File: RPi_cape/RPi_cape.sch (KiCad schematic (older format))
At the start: 110 parts, among them J1 Conn_01x04, J10 Conn_01x02, J11 Conn_01x02, J12 Conn_01x02, J15 Conn_01x06, J16 Conn_01x06, J2 Conn_01x02, J21 Conn_01x06, J3 Conn_01x02, J4 Conn_01x02, J5 Conn_01x03, J6 Conn_01x03, J7 Conn_01x02, J8 Conn_02x20_Odd_Even, J9 Conn_01x02, U1 TL431A, U2 ADC128D818, U3 ADC128D818

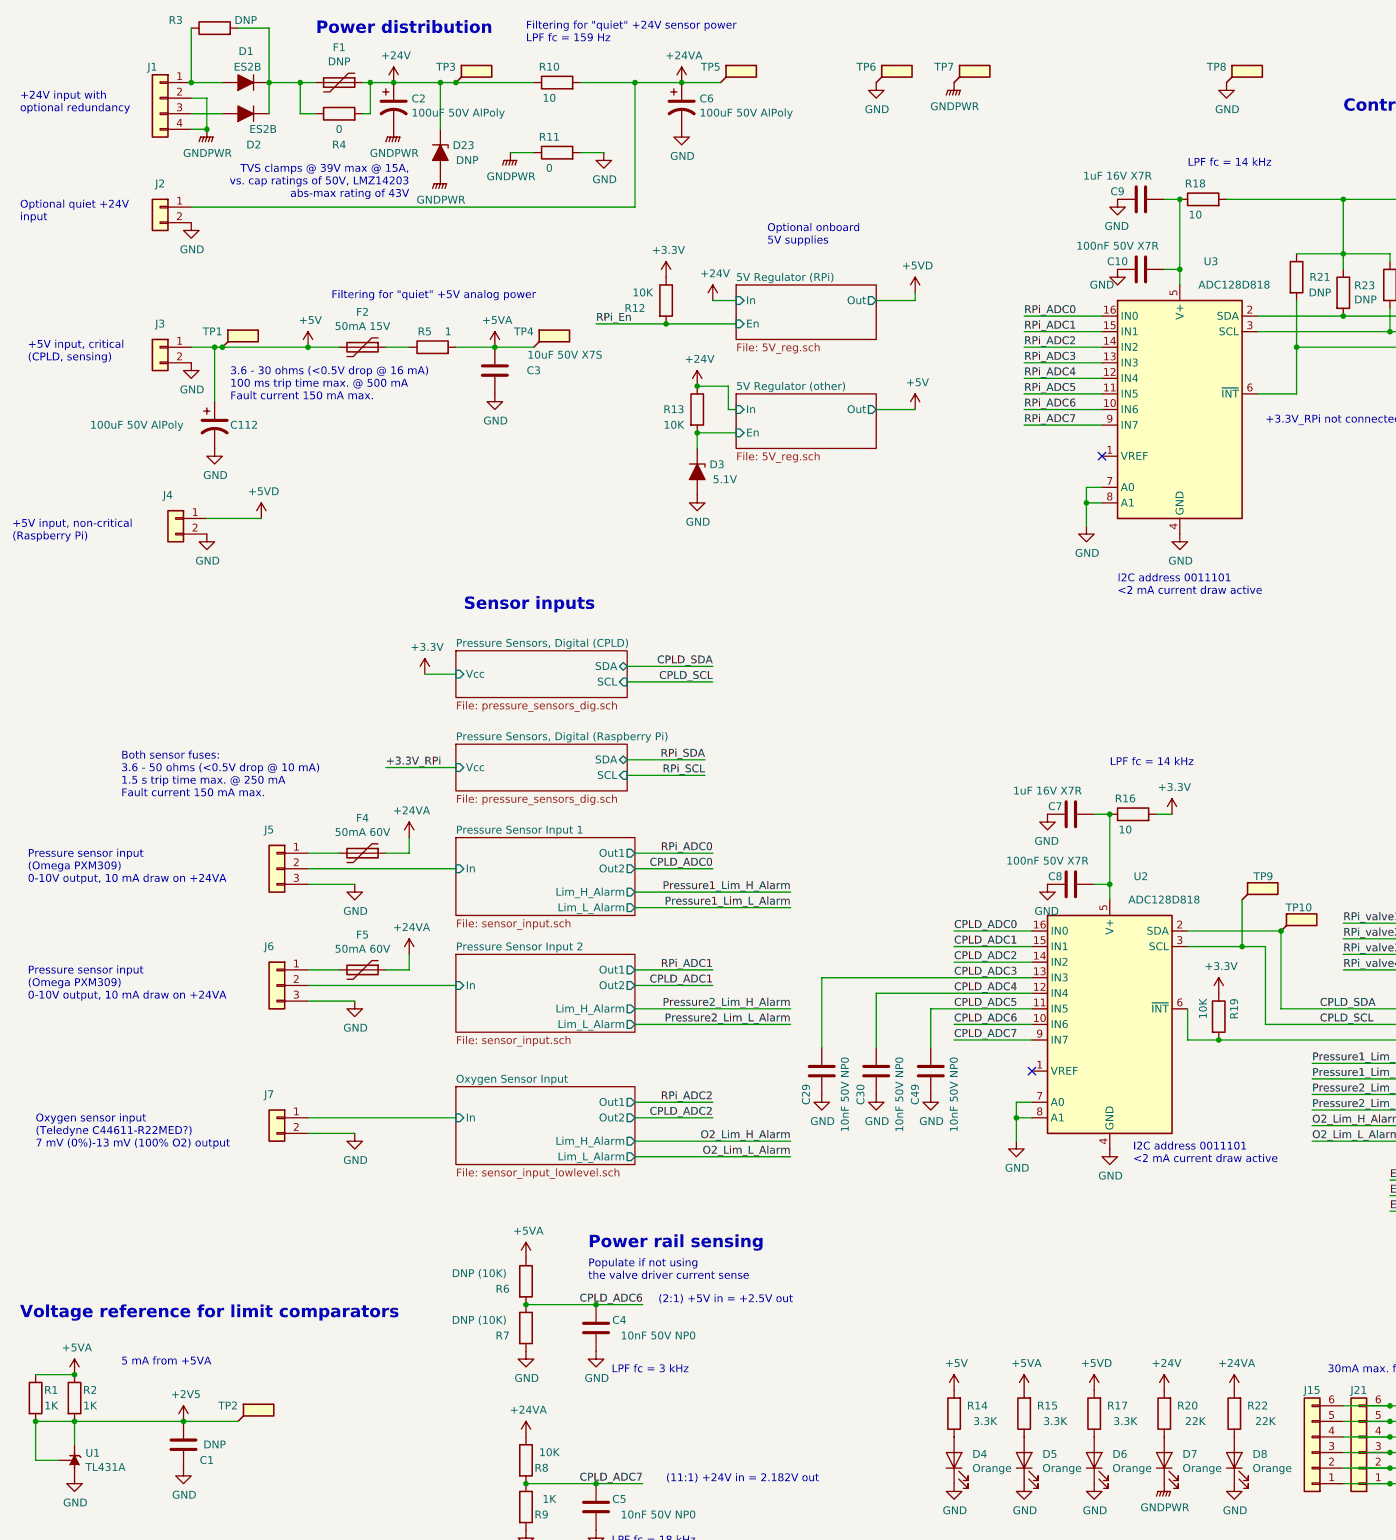
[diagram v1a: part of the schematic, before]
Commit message: Updates based on testing, extra documentation
Added thermal calculations, possible thermal-induced problems to fault-condition list
Renamed error calculations file
Added some bringup tests
Changed 24V LED resistors (R20, R22) to 24.9K to consolidate BOM
Adjusted audio amp volume and filtering according to breadboard experiments
Moved bottom-end mounting holes and encoder connectors to avoid interfering mechanically with Raspberry Pi
Replaced under-sized power-ORing diodes with better Schottky option, added heatsinking with copper planes
Improved LMZ14203 heatsinking by removing thermal reliefs, re-arranging input-current-measurement testpoints to increase top-layer copper area
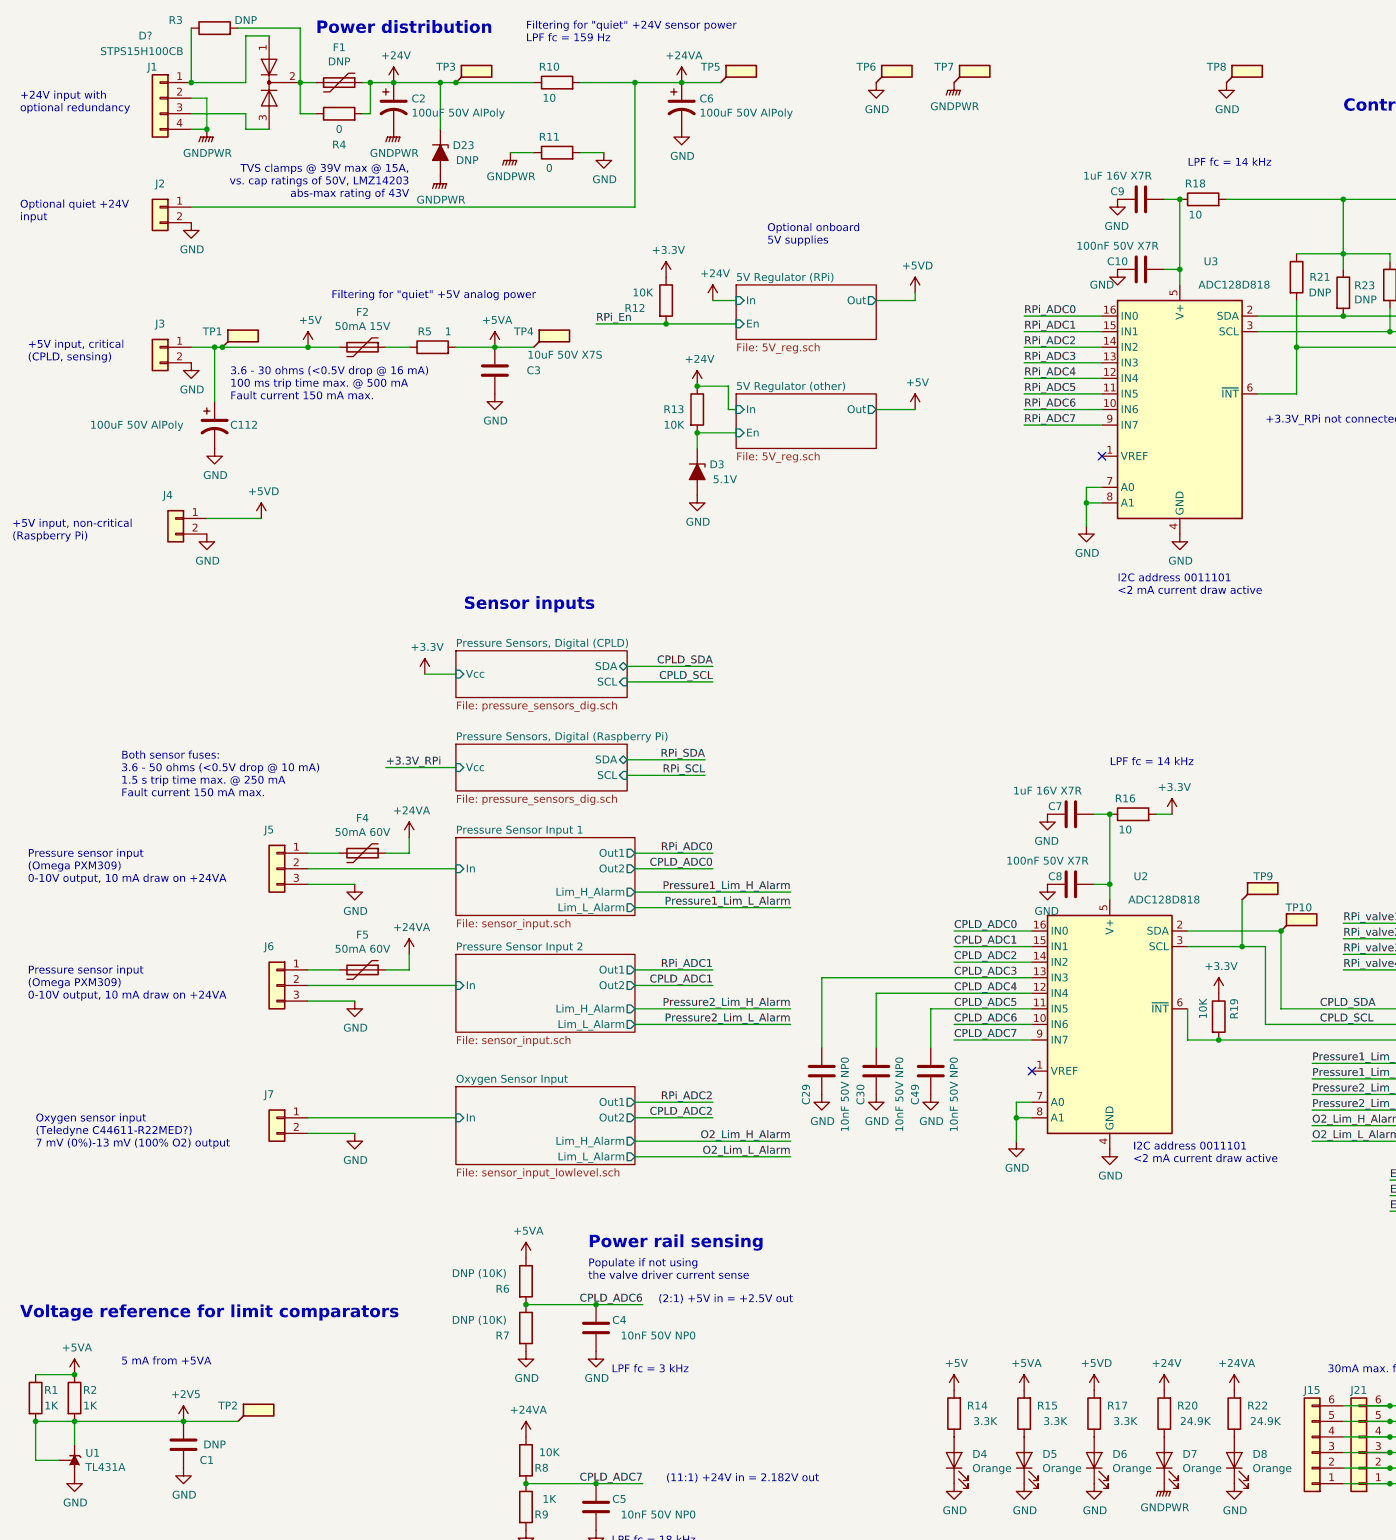
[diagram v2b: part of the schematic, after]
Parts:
- removed D1, D2: ES2B, Ventilator:D_SMA, symbol Device:D_ALT
- added D?: STPS15H100CB, Package_TO_SOT_SMD:TO-252-2, symbol Device:D_x2_KCom_AKA
- R20, R22: value 22K -> 24.9K; Part Number RK73H2BTTD2202F -> RK73H2BTTD2492F
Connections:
- net at J1.1 (Pin_1), R3.1: now also D?.1 (A)
- net at J1.3 (Pin_3): now also D?.3 (A)
- net at F1.2, R3.2, R4.1: now also D?.2 (K)
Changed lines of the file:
@@
 Title "Raspberry Pi Hat for JamVent Adaptation"
 Date ""
-Rev "1.8"
+Rev "1.9"
 Comp "US JamVent Team"
 Comment1 "Don Straney"
@@
 Connection ~ 1750 1250
 $Comp
-L Device:D_ALT D?
-U 1 1 5E93929F
-P 2000 950
-AR Path="/5E8FBD97/5E93929F" Ref="D?"  Part="1"
-AR Path="/5E8DEDC0/5E93929F" Ref="D?"  Part="1"
-AR Path="/5E8DFCAD/5E93929F" Ref="D?"  Part="1"
-AR Path="/5E8E0754/5E93929F" Ref="D?"  Part="1"
-AR Path="/5E93929F" Ref="D1"  Part="1"
-F 0 "D1" H 1950 750 50  0000 L CNN
-F 1 "ES2B" H 1900 850 50  0000 L CNN
-F 2 "Ventilator:D_SMA" H 2000 950 50  0001 C CNN
-F 3 "~" H 2000 950 50  0001 C CNN
-F 4 "Vishay" H 2000 950 50  0001 C CNN "Manufacturer"
-F 5 "ES2G-E3/52T" H 2000 950 50  0001 C CNN "Part Number"
-	1    2000 950
-	-1   0    0    1
-$EndComp
-Wire Wire Line
-	1850 950  1650 950
-$Comp
-L Device:D_ALT D?
-U 1 1 5E93B9F0
-P 2000 1150
-AR Path="/5E8FBD97/5E93B9F0" Ref="D?"  Part="1"
-AR Path="/5E8DEDC0/5E93B9F0" Ref="D?"  Part="1"
-AR Path="/5E8DFCAD/5E93B9F0" Ref="D?"  Part="1"
-AR Path="/5E8E0754/5E93B9F0" Ref="D?"  Part="1"
-AR Path="/5E93B9F0" Ref="D2"  Part="1"
-F 0 "D2" H 1900 1350 50  0000 L CNN
-F 1 "ES2B" H 1800 1250 50  0000 L CNN
-F 2 "Ventilator:D_SMA" H 2000 1150 50  0001 C CNN
-F 3 "~" H 2000 1150 50  0001 C CNN
-F 4 "Vishay" H 2000 1150 50  0001 C CNN "Manufacturer"
-F 5 "ES2G-E3/52T" H 2000 1150 50  0001 C CNN "Part Number"
-	1    2000 1150
-	-1   0    0    1
-$EndComp
-Wire Wire Line
-	1650 1150 1850 1150
-Wire Wire Line
-	2150 1150 2150 950
-Wire Wire Line
-	2150 950  2350 950
-Connection ~ 2150 950
-$Comp
 L Device:R R10
 U 1 1 5E9432CB
@@
 $EndComp
 Wire Wire Line
-	1950 600  2150 600
-Wire Wire Line
-	2150 600  2150 950
-Wire Wire Line
 	1650 600  1650 950
 Connection ~ 1650 950
@@
 AR Path="/5E8C8865/5F731777" Ref="R?"  Part="1"
 F 0 "R20" H 7750 9450 50  0000 C CNN
-F 1 "22K" H 7700 9550 50  0000 C CNN
+F 1 "24.9K" H 7700 9550 50  0000 C CNN
 F 2 "Resistor_SMD:R_1206_3216Metric" V 7830 9500 50  0001 C CNN
 F 3 "~" H 7900 9500 50  0001 C CNN
 F 4 "KOA Speer" H 7900 9500 50  0001 C CNN "Manufacturer"
-F 5 "RK73H2BTTD2202F" H 7900 9500 50  0001 C CNN "Part Number"
+F 5 "RK73H2BTTD2492F" H 7900 9500 50  0001 C CNN "Part Number"
 	1    7900 9500
 	-1   0    0    1
@@
 AR Path="/5E8C8865/5F747055" Ref="R?"  Part="1"
 F 0 "R22" H 8200 9450 50  0000 C CNN
-F 1 "22K" H 8150 9550 50  0000 C CNN
+F 1 "24.9K" H 8150 9550 50  0000 C CNN
 F 2 "Resistor_SMD:R_1206_3216Metric" V 8280 9500 50  0001 C CNN
 F 3 "~" H 8350 9500 50  0001 C CNN
 F 4 "KOA Speer" H 8350 9500 50  0001 C CNN "Manufacturer"
-F 5 "RK73H2BTTD2202F" H 8350 9500 50  0001 C CNN "Part Number"
+F 5 "RK73H2BTTD2492F" H 8350 9500 50  0001 C CNN "Part Number"
 	1    8350 9500
 	-1   0    0    1
@@
 Wire Wire Line
 	9350 9950 9700 9950
+$Comp
+L Device:D_x2_KCom_AKA D?
+U 1 1 5EC00ED4
+P 2150 950
+F 0 "D?" V 1850 1700 50  0000 L CNN
+F 1 "STPS15H100CB" V 1950 1500 50  0000 L CNN
+F 2 "Package_TO_SOT_SMD:TO-252-2" H 2150 950 50  0001 C CNN
+F 3 "~" H 2150 950 50  0001 C CNN
+F 4 "ST" V 2150 950 50  0001 C CNN "Manufacturer"
+F 5 "STPS15H100CB-TR" V 2150 950 50  0001 C CNN "Part Number"
+	1    2150 950
+	0    -1   1    0
+$EndComp
+Wire Wire Line
+	2350 600  2350 950
+Wire Wire Line
+	1950 600  2350 600
+Wire Wire Line
+	2000 950  2000 650
+Wire Wire Line
+	2000 650  2150 650
+Wire Wire Line
+	1650 950  2000 950
+Wire Wire Line
+	2000 1150 2000 1250
+Wire Wire Line
+	2000 1250 2150 1250
+Wire Wire Line
+	1650 1150 2000 1150
 $EndSCHEMATC

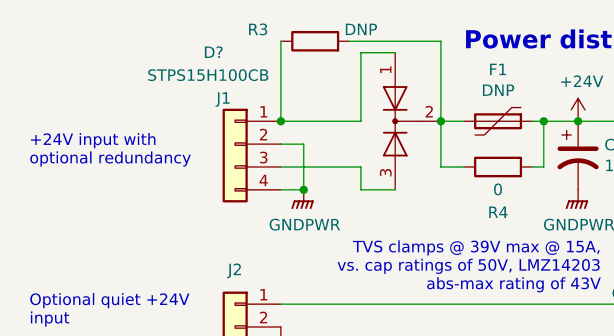
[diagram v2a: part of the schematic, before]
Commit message: Cleanup, manufacturing
Added doc on differences between 'proto' version and 'full' version
Added manufacturing README in proto version
Removed unused hardwired-limited O2 alarm nets in proto version
Fixed missed-annotation on D1 in full version
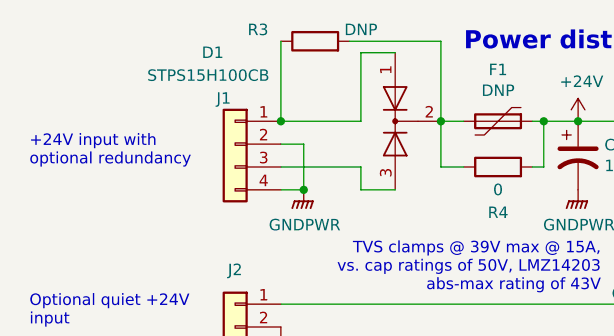
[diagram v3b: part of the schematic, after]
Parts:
- gave numbers to parts that had none: 1
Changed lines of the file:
@@
 	9350 9950 9700 9950
 $Comp
-L Device:D_x2_KCom_AKA D?
+L Device:D_x2_KCom_AKA D1
 U 1 1 5EC00ED4
 P 2150 950
-F 0 "D?" V 1850 1700 50  0000 L CNN
+F 0 "D1" V 1850 1700 50  0000 L CNN
 F 1 "STPS15H100CB" V 1950 1500 50  0000 L CNN
 F 2 "Package_TO_SOT_SMD:TO-252-2" H 2150 950 50  0001 C CNN
